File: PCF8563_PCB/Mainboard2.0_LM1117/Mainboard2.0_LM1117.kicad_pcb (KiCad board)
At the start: 2 copper layers, 40 parts, among them J1 USB_B, J2 CONN_01X03, J3 CONN_01X03, J4 CONN_01X02, J5 CONN_01X02, J6 SD_Card, Q1 BC847, Q2 BC847, SW1 SW_DIP_x01, U1 FT232RL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

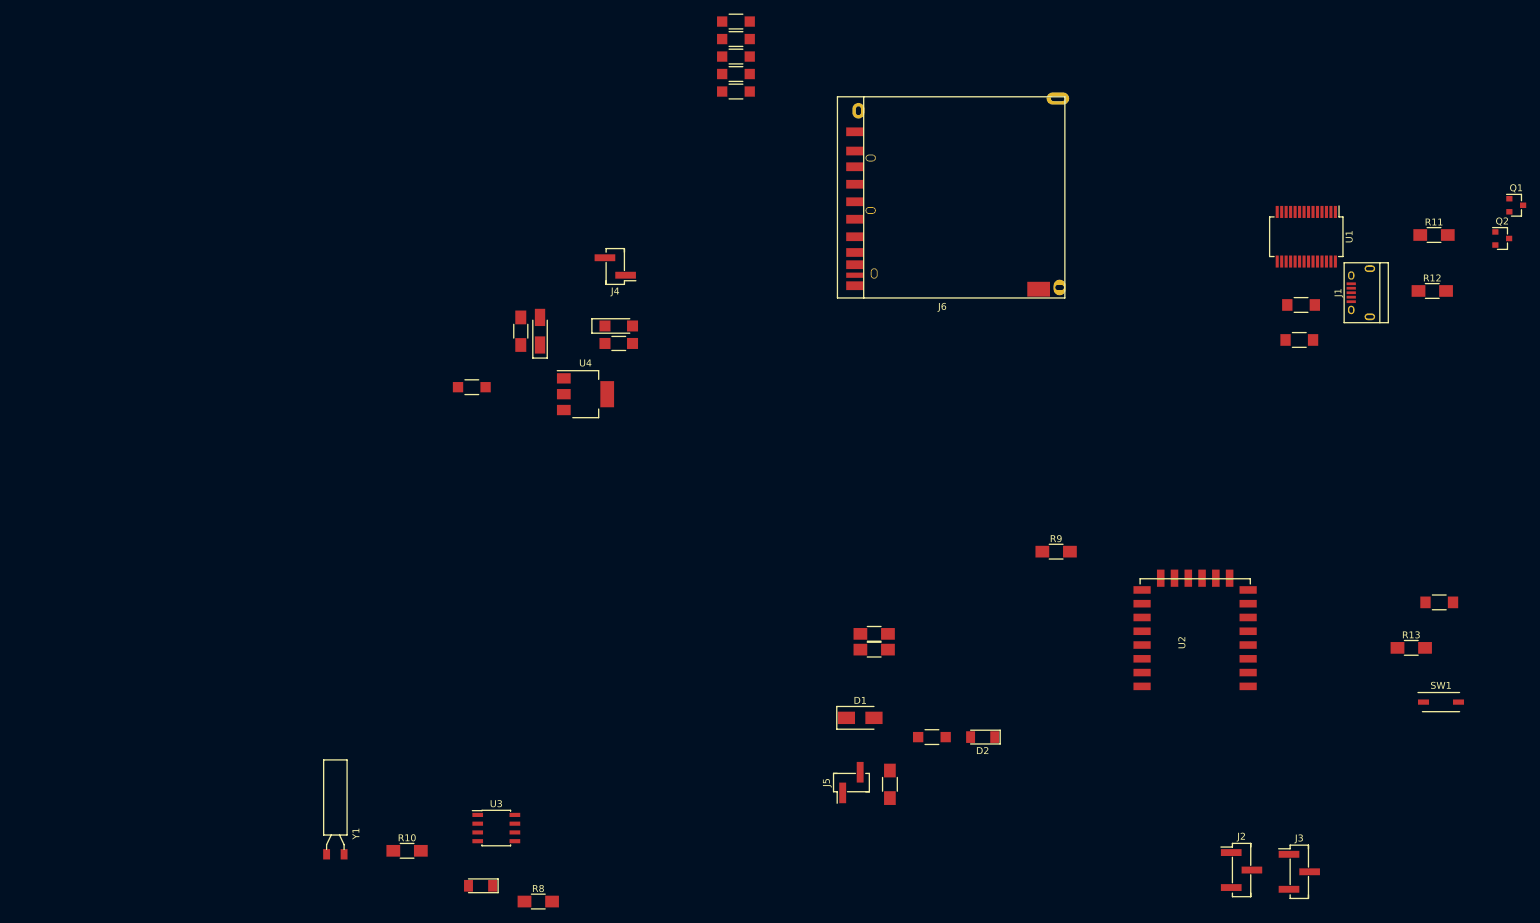
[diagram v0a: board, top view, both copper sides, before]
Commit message: PCB work
Need to remove 1.1 files from 2.0 folder
Fixed component enumeration so PCB rework will be easier
Still need to finish new PCB
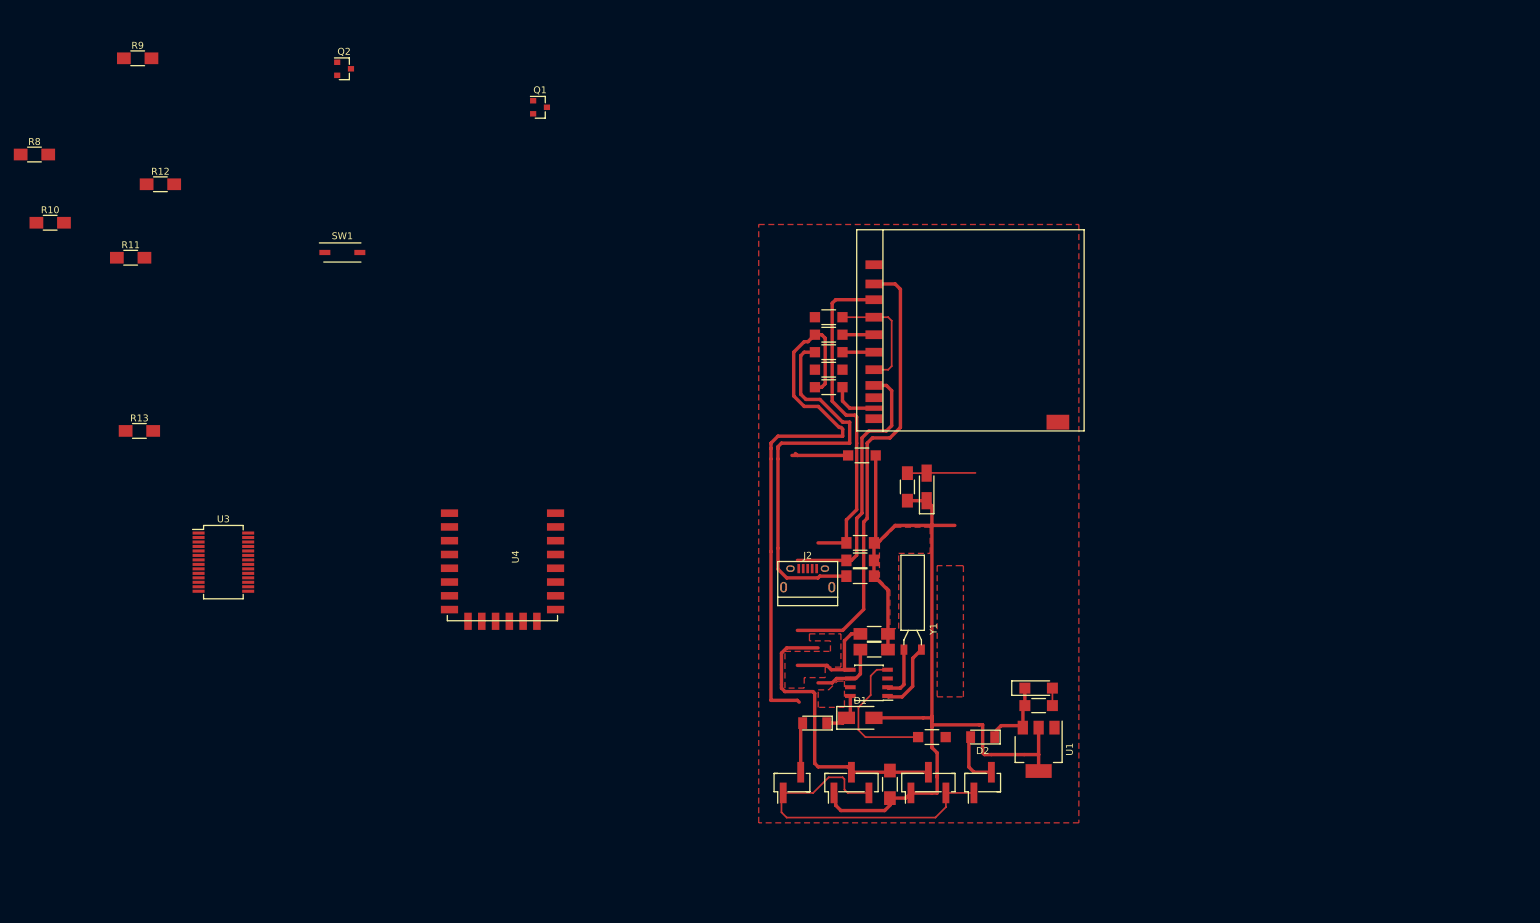
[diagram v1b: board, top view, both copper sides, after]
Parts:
- removed J3: CONN_01X03, Pin_Headers:Pin_Header_Straight_1x03_Pitch2.54mm_SMD_Pin1Left
- added J7: CONN_01X02, Pin_Headers:Pin_Header_Straight_1x02_Pitch2.54mm_SMD_Pin1Left, F.Cu at (162.6, 133.9)
- D1: value 1N4007 -> 1N4148
- D2: value 1N4148 -> 1N4007
- J1: value USB_B -> CONN_01X03; footprint Connectors:USB_Micro-B -> Pin_Headers:Pin_Header_Straight_1x03_Pitch2.54mm_SMD_Pin1Left
- J2: value CONN_01X03 -> USB_B; footprint Pin_Headers:Pin_Header_Straight_1x03_Pitch2.54mm_SMD_Pin1Left -> Connectors:USB_Micro-B
- J4: value CONN_01X02 -> SD_Card; footprint Pin_Headers:Pin_Header_Straight_1x02_Pitch2.54mm_SMD_Pin1Left -> Moje:SDCARD-STANDARD
- J5: value CONN_01X02 -> CONN_01X03; footprint Pin_Headers:Pin_Header_Straight_1x02_Pitch2.54mm_SMD_Pin1Left -> Pin_Headers:Pin_Header_Straight_1x03_Pitch2.54mm_SMD_Pin1Left
- J6: value SD_Card -> CONN_01X02; footprint Moje:SDCARD-STANDARD -> Pin_Headers:Pin_Header_Straight_1x02_Pitch2.54mm_SMD_Pin1Left
- R1: value 4k7 -> 10k
- R10: value 4k7 -> 1k
- R5, R6: value 10k -> 4k7
- R9: value 1k -> 10k
- U1: value FT232RL -> LM1117-3.3; footprint Housings_SSOP:SSOP-28_5.3x10.2mm_Pitch0.65mm -> TO_SOT_Packages_SMD:SOT-223-3Lead_TabPin2
- U2: value ESP-12E -> PCF8563; footprint ESP8266:ESP-12E_SMD -> Housings_SOIC:SOIC-8_3.9x4.9mm_Pitch1.27mm
- U3: value PCF8563 -> FT232RL; footprint Housings_SOIC:SOIC-8_3.9x4.9mm_Pitch1.27mm -> Housings_SSOP:SSOP-28_5.3x10.2mm_Pitch0.65mm
- U4: value LM1117-3.3 -> ESP-12E; footprint TO_SOT_Packages_SMD:SOT-223-3Lead_TabPin2 -> ESP8266:ESP-12E_SMD
- moved R11 189.3 mm to (38.9, 57.7)
- moved R13 187.3 mm to (40.1, 82.8)
- moved R12 185.3 mm to (43.2, 47.0)
- moved SW1 172.4 mm to (69.6, 56.9)
- moved Q2 169.9 mm to (69.8, 30.2)
- moved R9 151.4 mm to (39.9, 28.7)
- moved Q1 142.4 mm to (98.3, 35.8)
- moved R8 130.8 mm to (24.9, 42.7)
- moved R10 104.9 mm to (27.2, 52.6)
- moved J6 95.7 mm to (134.9, 133.9), turned to 90 degrees
- moved J1 94.8 mm to (154.7, 133.9)
- moved Y1 88.9 mm to (153.7, 114.6)
- moved R3 84.2 mm to (144.8, 103.9)
- moved U1 84.0 mm to (170.7, 129.0)
- moved C1 80.5 mm to (170.7, 122.7)
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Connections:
- D1 pad 1: Net-(C1-Pad1) -> Net-(D1-Pad1)
- D1 pad 2: Net-(D1-Pad2) -> 3V3
- D2 pad 1: Net-(D2-Pad1) -> Net-(C1-Pad1)
- D3 pad 1: Net-(D2-Pad1) -> Net-(D1-Pad1)
- D3 pad 2: 3V3 -> Net-(D3-Pad2)
- J1 pad 1: Net-(J1-Pad1) -> 3V3
- J1 pad 2: Net-(J1-Pad2) -> 1wire
- J1 pad 3: Net-(J1-Pad3) -> GND
- J2 pad 1: 3V3 -> Net-(J2-Pad1)
- J2 pad 2: 1wire -> Net-(J2-Pad2)
- J2 pad 3: GND -> Net-(J2-Pad3)
- J4 pad 1: GND -> CS
- J4 pad 2: Net-(D1-Pad2) -> GPIO13
- J5 pad 1: GND -> 3V3
- J5 pad 2: Net-(D2-Pad2) -> 1wire
- J6 pad 1: CS -> GND
- J6 pad 2: GPIO13 -> Net-(D3-Pad2)
- R1 pad 1: Net-(R1-Pad1) -> 3V3
- R1 pad 2: Net-(J1-Pad1) -> GPIO13
- R10 pad 1: 3V3 -> Net-(R10-Pad1)
- R10 pad 2: GPIO4 -> 3V3
- R2 pad 1: GND -> 3V3
- R2 pad 2: Net-(R1-Pad1) -> GPIO12
- R3 pad 2: GPIO16 -> GPIO14
- R4 pad 2: GPIO13 -> GPIO16
- R5 pad 2: GPIO12 -> 1wire
- R6 pad 2: GPIO14 -> GPIO5
- R7 pad 2: 1wire -> GPIO4
- R8 pad 1: 3V3 -> Net-(R8-Pad1)
- R8 pad 2: GPIO5 -> Net-(J2-Pad1)
- R9 pad 1: Net-(R9-Pad1) -> GND
- R9 pad 2: 3V3 -> Net-(R8-Pad1)
- RJ6 pad 2: Net-(J6-Pad10) -> Net-(J4-Pad10)
- U1 pad 1: Rx -> GND
- U1 pad 2: DTR -> 3V3
- U1 pad 3: RTS -> Net-(C1-Pad1)
- U2 pad 1: RESET -> Net-(U2-Pad1)
- U2 pad 2: (no net) -> Net-(U2-Pad2)
- U2 pad 3: Net-(R9-Pad1) -> (no net)
- U2 pad 4: GPIO16 -> GND
- U2 pad 5: GPIO14 -> GPIO5
- U2 pad 6: GPIO12 -> GPIO4
- U2 pad 7: GPIO13 -> (no net)
- U2 pad 8: 3V3 -> Net-(D1-Pad1)
- U3 pad 1: Net-(U3-Pad1) -> Rx
- U3 pad 2: Net-(U3-Pad2) -> DTR
- U3 pad 3: (no net) -> RTS
- U3 pad 4: GND -> 3V3
- U3 pad 5: GPIO5 -> Tx
- U3 pad 6: GPIO4 -> (no net)
- U3 pad 7: (no net) -> GND
- U3 pad 8: Net-(D2-Pad1) -> (no net)
- U4 pad 1: GND -> RESET
- U4 pad 2: 3V3 -> (no net)
- U4 pad 3: Net-(C1-Pad1) -> Net-(R10-Pad1)
- Y1 pad 1: Net-(U3-Pad1) -> Net-(U2-Pad1)
- Y1 pad 2: Net-(U3-Pad2) -> Net-(U2-Pad2)
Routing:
- net 3V3: track 0.00 -> 155.7 mm
- net GND: track 0.00 -> 104.6 mm
- net GPIO16: track 0.00 -> 81.6 mm
- net CS: track 0.00 -> 65.2 mm
- net GPIO14: track 0.00 -> 58.7 mm
- net GPIO13: track 0.00 -> 48.1 mm
- net 1wire: track 0.00 -> 43.7 mm
- net GPIO12: track 0.00 -> 39.3 mm
- net GPIO5: track 0.00 -> 14.9 mm
- net Net-(C1-Pad1): track 0.00 -> 10.7 mm
- net GPIO4: track 0.00 -> 10.2 mm
- net Net-(U2-Pad1): track 0.00 -> 10.2 mm
- net Net-(D2-Pad2): track 0.00 -> 7.93 mm
- net Net-(U2-Pad2): track 0.00 -> 7.72 mm
- net Net-(D3-Pad2): track 0.00 -> 7.25 mm
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- added copper zone on F.Cu, net (none)
- added copper zone on F.Cu, net GND

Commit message: Minor code changes
Little cleanup
Cosmetic changes
Added keywords for Czas.h library and moved to it's own directory (otherwise keywords won't work)
Removed unnescesary crap I forgot to remove earlier
Updated description in README for PCF8563_JSON
Updated SettingsGenerator for newest JSON
Had a little fun with new PCB but I don't think it's gonna work out
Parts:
- moved J2 95.0 mm to (43.2, 118.1)
- moved Q2 47.5 mm to (74.9, 77.5)
- moved Q1 44.5 mm to (74.9, 73.7)
- moved R12 40.4 mm to (71.1, 76.2), turned to 90 degrees
- moved R11 35.0 mm to (68.6, 76.2), turned to 270 degrees
- moved R13 32.5 mm to (72.4, 86.4)
- moved SW1 25.8 mm to (72.4, 82.5), turned to 180 degrees
- moved U4 17.9 mm to (81.3, 77.5)
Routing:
- net 1wire: track 43.7 -> 68.7 mm
- net RESET: track 0.00 -> 14.9 mm
- net 3V3: track 155.7 -> 169.8 mm
- net RTS: track 0.00 -> 8.59 mm
- net Net-(Q1-Pad1): track 0.00 -> 7.29 mm
- net Net-(Q2-Pad1): track 0.00 -> 3.93 mm
- net DTR: track 0.00 -> 2.98 mm
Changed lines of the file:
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@@
   (general
     (links 93)
-    (no_connects 55)
-    (area 0 0 0 0)
+    (no_connects 46)
+    (area 21.416999 25.877 177.567001 139.700001)
     (thickness 1.6)
     (drawings 2)
-    (tracks 223)
+    (tracks 249)
     (zones 0)
     (modules 40)
@@
   )
   (module Connectors:USB_Micro-B (layer F.Cu)
-    (at 137.16 104.14)
+    (at 43.18 118.11)
     (descr "Micro USB Type B Receptacle")
     (tags "USB USB_B USB_micro USB_OTG")
@@
   )
   (module TO_SOT_Packages_SMD:SOT-23 (layer F.Cu)
-    (at 98.298 35.814)
+    (at 74.93 73.66)
     (descr "SOT-23, Standard")
     (tags SOT-23)
@@
   )
   (module TO_SOT_Packages_SMD:SOT-23 (layer F.Cu)
-    (at 69.85 30.226)
+    (at 74.93 77.47)
     (descr "SOT-23, Standard")
     (tags SOT-23)
@@
   )
   (module Resistors_SMD:R_1206_HandSoldering (layer F.Cu)
-    (at 38.862 57.658)
+    (at 68.58 76.2 270)
     (descr "Resistor SMD 1206, hand soldering")
     (tags "resistor 1206")
     (attr smd)
-    (fp_text reference R11 (at 0 -1.85) (layer F.SilkS)
-      (effects (font (size 1 1) (thickness 0.15)))
-    )
-    (fp_text value 10k (at 0 1.9) (layer F.Fab)
-      (effects (font (size 1 1) (thickness 0.15)))
-    )
-    (fp_text user %R (at 0 0) (layer F.Fab)
+    (fp_text reference R11 (at 0 -1.85 270) (layer F.SilkS)
+      (effects (font (size 1 1) (thickness 0.15)))
+    )
+    (fp_text value 10k (at 0 1.9 270) (layer F.Fab)
+      (effects (font (size 1 1) (thickness 0.15)))
+    )
+    (fp_text user %R (at 0 0 270) (layer F.Fab)
       (effects (font (size 0.7 0.7) (thickness 0.105)))
     )
@@
     (fp_line (start 3.25 1.1) (end 3.25 -1.11) (layer F.CrtYd) (width 0.05))
     (fp_line (start 3.25 1.1) (end -3.25 1.1) (layer F.CrtYd) (width 0.05))
-    (pad 1 smd rect (at -2 0) (size 2 1.7) (layers F.Cu F.Paste F.Mask)
+    (pad 1 smd rect (at -2 0 270) (size 2 1.7) (layers F.Cu F.Paste F.Mask)
       (net 16 "Net-(Q1-Pad1)"))
-    (pad 2 smd rect (at 2 0) (size 2 1.7) (layers F.Cu F.Paste F.Mask)
+    (pad 2 smd rect (at 2 0 270) (size 2 1.7) (layers F.Cu F.Paste F.Mask)
       (net 19 RTS))
     (model ${KISYS3DMOD}/Resistors_SMD.3dshapes/R_1206.wrl
@@
   )
   (module Resistors_SMD:R_1206_HandSoldering (layer F.Cu)
-    (at 43.18 46.99)
+    (at 71.12 76.2 90)
     (descr "Resistor SMD 1206, hand soldering")
     (tags "resistor 1206")
     (attr smd)
-    (fp_text reference R12 (at 0 -1.85) (layer F.SilkS)
-      (effects (font (size 1 1) (thickness 0.15)))
-    )
-    (fp_text value 10k (at 0 1.9) (layer F.Fab)
-      (effects (font (size 1 1) (thickness 0.15)))
-    )
-    (fp_text user %R (at 0 0) (layer F.Fab)
+    (fp_text reference R12 (at 0 -1.85 90) (layer F.SilkS)
+      (effects (font (size 1 1) (thickness 0.15)))
+    )
+    (fp_text value 10k (at 0 1.9 90) (layer F.Fab)
+      (effects (font (size 1 1) (thickness 0.15)))
+    )
+    (fp_text user %R (at 0 0 90) (layer F.Fab)
       (effects (font (size 0.7 0.7) (thickness 0.105)))
     )
@@
     (fp_line (start 3.25 1.1) (end 3.25 -1.11) (layer F.CrtYd) (width 0.05))
     (fp_line (start 3.25 1.1) (end -3.25 1.1) (layer F.CrtYd) (width 0.05))
-    (pad 1 smd rect (at -2 0) (size 2 1.7) (layers F.Cu F.Paste F.Mask)
+    (pad 1 smd rect (at -2 0 90) (size 2 1.7) (layers F.Cu F.Paste F.Mask)
       (net 18 "Net-(Q2-Pad1)"))
-    (pad 2 smd rect (at 2 0) (size 2 1.7) (layers F.Cu F.Paste F.Mask)
+    (pad 2 smd rect (at 2 0 90) (size 2 1.7) (layers F.Cu F.Paste F.Mask)
       (net 17 DTR))
     (model ${KISYS3DMOD}/Resistors_SMD.3dshapes/R_1206.wrl
@@
   )
   (module Resistors_SMD:R_1206_HandSoldering (layer F.Cu)
-    (at 40.132 82.804)
+    (at 72.39 86.36)
     (descr "Resistor SMD 1206, hand soldering")
     (tags "resistor 1206")
@@
   )
   (module Buttons_Switches_SMD:SW_DIP_x1_W5.08mm_Slide_Copal_CHS-A (layer F.Cu)
-    (at 69.596 56.896)
+    (at 72.39 82.55 180)
     (descr "1x-dip-switch, Slide, row spacing 5.08 mm (200 mils), Copal_CHS-A")
     (tags "DIP Switch Slide 5.08mm 200mil Copal_CHS-A")
     (attr smd)
-    (fp_text reference SW1 (at 0 -2.39) (layer F.SilkS)
-      (effects (font (size 1 1) (thickness 0.15)))
-    )
-    (fp_text value SW_DIP_x01 (at 0 2.39) (layer F.Fab)
+    (fp_text reference SW1 (at 0 -2.39 180) (layer F.SilkS)
+      (effects (font (size 1 1) (thickness 0.15)))
+    )
+    (fp_text value SW_DIP_x01 (at 0 2.39 180) (layer F.Fab)
       (effects (font (size 1 1) (thickness 0.15)))
     )
@@
     (fp_line (start 3.6 1.7) (end 3.6 -1.7) (layer F.CrtYd) (width 0.05))
     (fp_line (start 3.6 -1.7) (end -3.6 -1.7) (layer F.CrtYd) (width 0.05))
-    (pad 1 smd rect (at -2.54 0) (size 1.6 0.76) (layers F.Cu F.Mask)
+    (pad 1 smd rect (at -2.54 0 180) (size 1.6 0.76) (layers F.Cu F.Mask)
       (net 20 RESET))
-    (pad 2 smd rect (at 2.54 0) (size 1.6 0.76) (layers F.Cu F.Mask)
+    (pad 2 smd rect (at 2.54 0 180) (size 1.6 0.76) (layers F.Cu F.Mask)
       (net 9 GND))
     (model Buttons_Switches_SMD.3dshapes/SW_DIP_x1_W5.08mm_Slide_Copal_CHS-A.wrl
@@
   )
   (module ESP8266:ESP-12E_SMD (layer F.Cu)
-    (at 85.852 94.742)
+    (at 81.28 77.47)
     (descr "Module, ESP-8266, ESP-12, 16 pad, SMD")
     (tags "Module ESP-8266 ESP8266")
@@
   (segment (start 164.56 126.27) (end 165.236 125.594) (width 0.5) (layer F.Cu) (net 1))
   (segment (start 164.56 127.254) (end 164.56 126.27) (width 0.5) (layer F.Cu) (net 1))
+  (segment (start 75.93 73.66) (end 82.55 73.66) (width 0.5) (layer F.Cu) (net 2))
+  (segment (start 93.09 85.47) (end 95.28 85.47) (width 0.5) (layer F.Cu) (net 2))
+  (segment (start 88.9 81.28) (end 93.09 85.47) (width 0.5) (layer F.Cu) (net 2))
+  (segment (start 88.9 80.01) (end 88.9 81.28) (width 0.5) (layer F.Cu) (net 2))
+  (segment (start 82.55 73.66) (end 88.9 80.01) (width 0.5) (layer F.Cu) (net 2))
   (segment (start 133.35 119.634) (end 133.35 120.142) (width 0.5) (layer F.Cu) (net 2))
   (segment (start 138.66 114.3) (end 134.112 114.3) (width 0.5) (layer F.Cu) (net 2))
@@
   (segment (start 143.764 132.358) (end 148.852 132.358) (width 0.5) (layer F.Cu) (net 2))
   (segment (start 148.852 132.358) (end 149.098 132.112) (width 0.5) (layer F.Cu) (net 2))
+  (segment (start 81.28 91.47) (end 73.69 91.47) (width 0.5) (layer F.Cu) (net 3) (status 400000))
+  (segment (start 70.39 88.17) (end 70.39 86.36) (width 0.5) (layer F.Cu) (net 3) (status 800000))
+  (segment (start 73.69 91.47) (end 70.39 88.17) (width 0.5) (layer F.Cu) (net 3))
   (segment (start 170.688 129.794) (end 168.588 129.794) (width 0.5) (layer F.Cu) (net 3))
   (segment (start 162.56 125.476) (end 162.56 129.54) (width 0.5) (layer F.Cu) (net 3))
@@
   (segment (start 142.78 101.6) (end 143.51 101.6) (width 0.5) (layer F.Cu) (net 15))
   (segment (start 142.78 101.6) (end 135.66 101.6) (width 0.5) (layer F.Cu) (net 15))
+  (segment (start 68.58 74.2) (end 68.58 72.39) (width 0.25) (layer F.Cu) (net 16))
+  (segment (start 72.71 72.71) (end 73.93 72.71) (width 0.25) (layer F.Cu) (net 16))
+  (segment (start 72.39 72.39) (end 72.71 72.71) (width 0.25) (layer F.Cu) (net 16))
+  (segment (start 68.58 72.39) (end 72.39 72.39) (width 0.25) (layer F.Cu) (net 16))
+  (segment (start 71.12 74.2) (end 73.52 74.2) (width 0.25) (layer F.Cu) (net 17))
+  (segment (start 73.52 74.2) (end 73.93 74.61) (width 0.25) (layer F.Cu) (net 17))
+  (segment (start 73.93 76.52) (end 72.07 76.52) (width 0.25) (layer F.Cu) (net 18))
+  (segment (start 72.07 76.52) (end 71.12 77.47) (width 0.25) (layer F.Cu) (net 18))
+  (segment (start 71.12 77.47) (end 71.12 78.2) (width 0.25) (layer F.Cu) (net 18))
+  (segment (start 68.58 78.2) (end 68.58 80.01) (width 0.25) (layer F.Cu) (net 19))
+  (segment (start 73.93 79.74) (end 73.93 78.42) (width 0.25) (layer F.Cu) (net 19))
+  (segment (start 73.66 80.01) (end 73.93 79.74) (width 0.25) (layer F.Cu) (net 19))
+  (segment (start 68.58 80.01) (end 73.66 80.01) (width 0.25) (layer F.Cu) (net 19))
+  (segment (start 74.93 82.55) (end 74.93 85.82) (width 0.25) (layer F.Cu) (net 20) (status C00000))
+  (segment (start 74.93 85.82) (end 74.39 86.36) (width 0.25) (layer F.Cu) (net 20) (status C00000))
+  (segment (start 75.93 77.47) (end 75.93 81.55) (width 0.25) (layer F.Cu) (net 20))
+  (segment (start 75.93 81.55) (end 74.93 82.55) (width 0.25) (layer F.Cu) (net 20))
+  (segment (start 81.28 77.47) (end 75.93 77.47) (width 0.25) (layer F.Cu) (net 20))
   (segment (start 132.842 85.344) (end 132.842 85.09) (width 0.5) (layer F.Cu) (net 21))
   (segment (start 132.842 99.822) (end 132.842 86.868) (width 0.5) (layer F.Cu) (net 21))
